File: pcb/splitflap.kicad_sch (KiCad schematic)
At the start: 84 parts, among them J1 Motor D, J10 Hall C, J11 Hall B, J12 I2C, J2 Motor C, J3 Motor B, J4 Motor A, J5 BarrelJack Vertical, J6 USB_C_Receptacle_USB2.0_16P, J7 BarrelJack Horizontal, J8 Hall A1, J9 Hall D, M1 28BYJ-48, SW1 A, SW2 B, SW3 Mode, SW4 RST, U1 ULN2803A, U12 LM2596S-5, U2 ULN2803A, U3 DS18B20, U4 ESP32-S3-WROOM-1, U5 Hall A1, U6 UART, U7 LD1117S33CTR, U8 DCF-77, U9 Hall A2

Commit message: Use 0603 for resistors and capacitors
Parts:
- added R7: 220, Resistor_SMD:R_0603_1608Metric, symbol Device:R
- C1, C10, C11, C12, C13, C14, C15, C17, C7: footprint Capacitor_SMD:C_0805_2012Metric_Pad1.18x1.45mm_HandSolder -> Capacitor_SMD:C_0603_1608Metric
- R1, R5: footprint Resistor_SMD:R_0805_2012Metric_Pad1.20x1.40mm_HandSolder -> Resistor_SMD:R_0603_1608Metric
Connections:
- net +3V3: now also C1.2, C17.2, R1.1, R5.1; no longer C1.1, C17.1, R1.2, R5.2
- net GND: now also C1.1, C17.1; no longer C1.2, C17.2
- net HALL_A1: now also R7.2; no longer R1.1, U5.2 (OUTPUT)
- net HALL_A2: now also R5.2; no longer R5.1
- new net: R1.2, R7.1, U5.2 (OUTPUT)

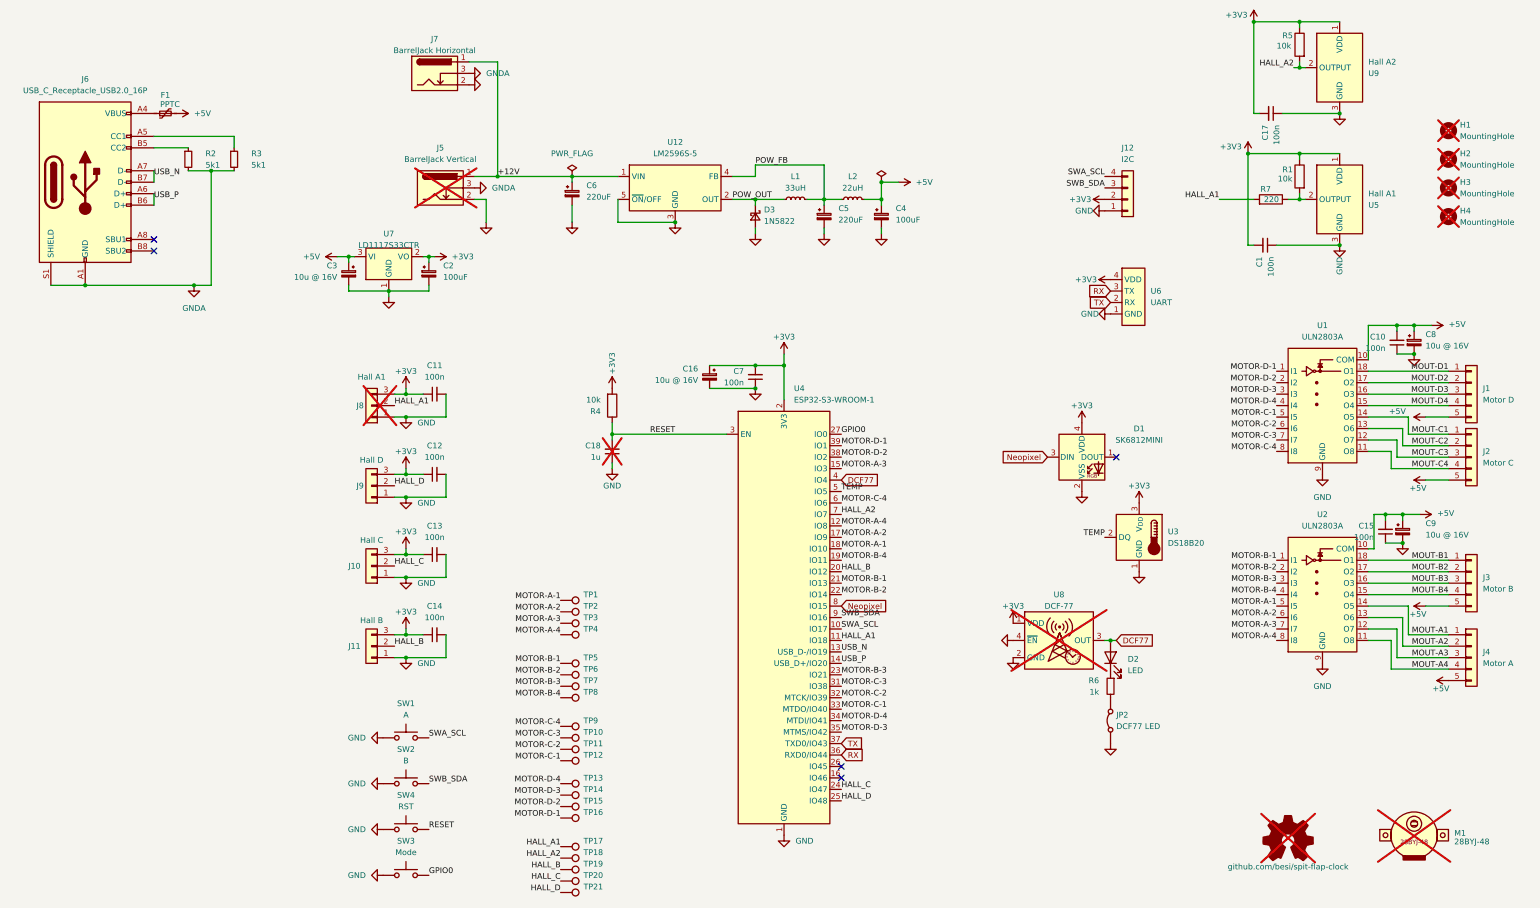
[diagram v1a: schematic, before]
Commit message: Update DNP field
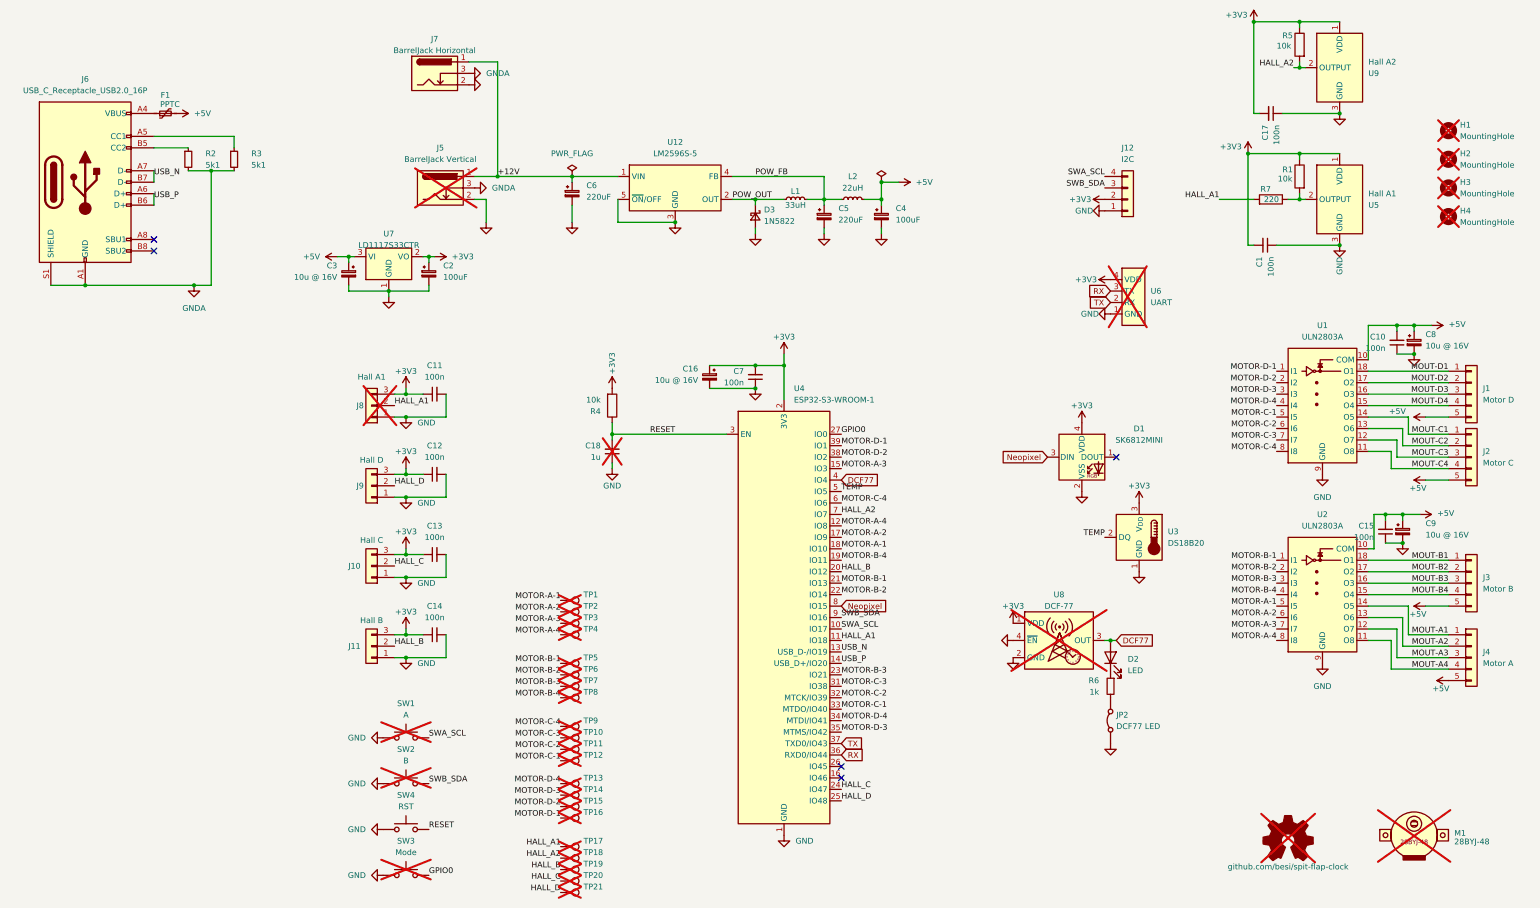
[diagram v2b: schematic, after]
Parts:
- D2, F1, J12, J6, J8, M1, R2, R3, R6, U3, U8: MPN (none) -> (none)
- SW1, SW2, SW3, U6: now not fitted
- TP1, TP10, TP11, TP12, TP13, TP14, TP15, TP16, TP17, TP18, TP19, TP2, TP20, TP21, TP3, TP4, TP5, TP6, TP7, TP8, TP9: MPN (none) -> (none); now not fitted

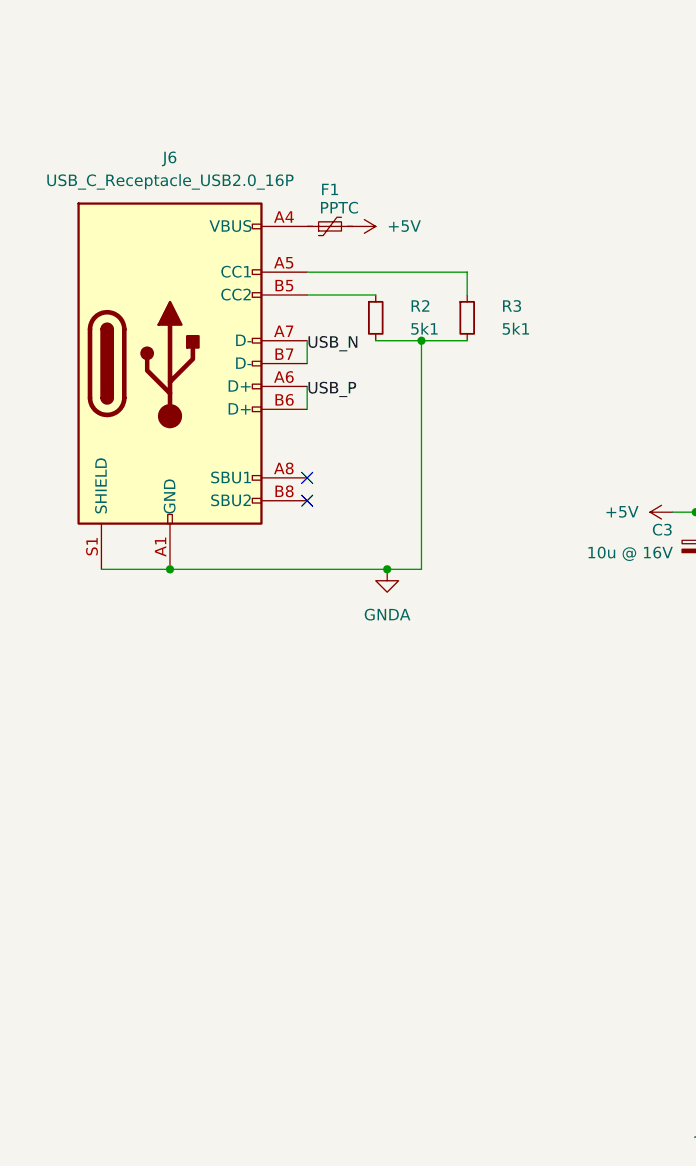
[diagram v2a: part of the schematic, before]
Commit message: Add ESD protection for the USB-C socket
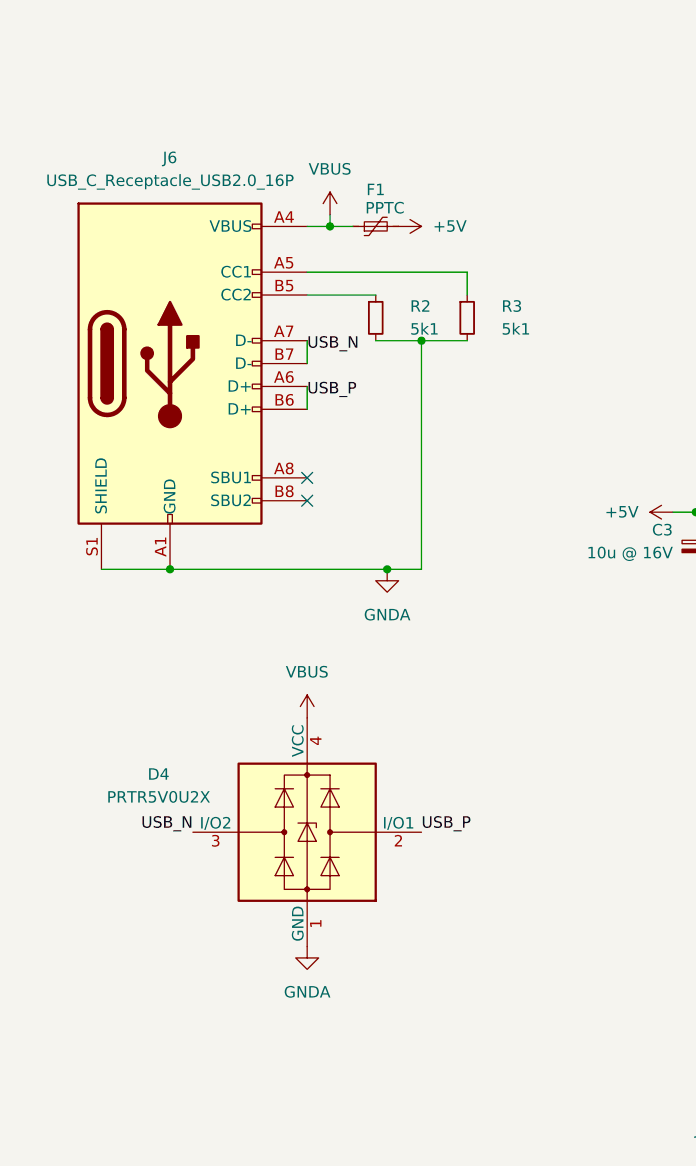
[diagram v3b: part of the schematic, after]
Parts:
- added D4: PRTR5V0U2X, Package_TO_SOT_SMD:SOT-143, symbol Power_Protection:PRTR5V0U2X
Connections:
- net GNDA: now also D4.1 (GND)
- net USB_N: now also D4.3 (I/O2)
- net USB_P: now also D4.2 (I/O1)
- net VBUS: now reaches F1.1, J6.A4 (VBUS), J6.A9 (VBUS), J6.B4 (VBUS), J6.B9 (VBUS)
- net VBUS: now also D4.4 (VCC)
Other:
- moved on the sheet: F1

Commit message: Change package of the temperature sensor
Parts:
- D4: MPN (none) -> PRTR5V0U2X
- J10, J11, J8, J9: MPN (none) -> B3B-PH-K-S
- J12: MPN (none) -> BM04B-SRSS-TB
- M1: MPN (none) -> 28BYJ-48
- SW1, SW2, SW3, SW4: MPN 434133025816 -> PTS815SJM250SMTRLFS
- U1, U2: MPN (none) -> ULN2803A
- U3: footprint Package_TO_SOT_THT:TO-92_Inline_Wide -> Package_TO_SOT_THT:TO-92S; MPN (none) -> 4518-DS18B20-ND
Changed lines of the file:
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@@
 			)
 		)
-		(property "MPN" " "
+		(property "MPN" "28BYJ-48"
 			(at 260.35 172.72 0)
 			(effects
@@
 			)
 		)
-		(property "MPN" "434133025816"
-			(at 36.83 161.29 0)
-			(effects
-				(font
-					(size 1.27 1.27)
-				)
-				(hide yes)
-			)
-		)
-		(property "Label1" ""
-			(at 36.83 161.29 0)
-			(effects
-				(font
-					(size 1.27 1.27)
-				)
-				(hide yes)
-			)
-		)
-		(property "Label2" ""
+		(property "MPN" "PTS815SJM250SMTRLFS"
 			(at 36.83 161.29 0)
 			(effects
@@
 			)
 		)
-		(property "MPN" " "
+		(property "MPN" "ULN2803A"
 			(at 240.03 116.84 0)
 			(effects
@@
 			)
 		)
-		(property "MPN" " "
+		(property "MPN" "B3B-PH-K-S "
 			(at 29.21 113.03 0)
 			(effects
@@
 			)
 		)
-		(property "MPN" "434133025816"
-			(at 36.83 151.13 0)
-			(effects
-				(font
-					(size 1.27 1.27)
-				)
-				(hide yes)
-			)
-		)
-		(property "Label1" ""
-			(at 36.83 151.13 0)
-			(effects
-				(font
-					(size 1.27 1.27)
-				)
-				(hide yes)
-			)
-		)
-		(property "Label2" ""
+		(property "MPN" "PTS815SJM250SMTRLFS"
 			(at 36.83 151.13 0)
 			(effects
@@
 			)
 		)
-		(property "MPN" " "
+		(property "MPN" "B3B-PH-K-S "
 			(at 29.21 130.81 0)
 			(effects
@@
 			)
 		)
-		(property "MPN" " "
+		(property "MPN" "ULN2803A"
 			(at 240.03 74.93 0)
 			(effects
@@
 			)
 		)
-		(property "MPN" " "
+		(property "MPN" "B3B-PH-K-S "
 			(at 29.21 77.47 0)
 			(effects
@@
 			)
 		)
-		(property "Footprint" "Package_TO_SOT_THT:TO-92_Inline_Wide"
+		(property "Footprint" "Package_TO_SOT_THT:TO-92S"
 			(at 224.79 113.03 0)
 			(effects
@@
 			)
 		)
-		(property "MPN" " "
+		(property "MPN" "4518-DS18B20-ND"
 			(at 199.39 106.68 0)
 			(effects
@@
 			)
 		)
+		(property "MPN" "PRTR5V0U2X"
+			(at -19.05 80.01 0)
+			(effects
+				(font
+					(size 1.27 1.27)
+				)
+				(hide yes)
+			)
+		)
 		(pin "4"
 		)
@@
 			)
 		)
-		(property "MPN" "434133025816"
-			(at 36.83 171.45 0)
-			(effects
-				(font
-					(size 1.27 1.27)
-				)
-				(hide yes)
-			)
-		)
-		(property "Label1" ""
-			(at 36.83 171.45 0)
-			(effects
-				(font
-					(size 1.27 1.27)
-				)
-				(hide yes)
-			)
-		)
-		(property "Label2" ""
+		(property "MPN" "PTS815SJM250SMTRLFS"
 			(at 36.83 171.45 0)
 			(effects
@@
 			)
 		)
-		(property "MPN" " "
+		(property "MPN" "B3B-PH-K-S "
 			(at 29.21 95.25 0)
 			(effects
@@
 			)
 		)
-		(property "MPN" " "
+		(property "MPN" "BM04B-SRSS-TB"
 			(at 196.85 31.75 0)
 			(effects
@@
 			)
 		)
-		(property "MPN" "434133025816"
-			(at 36.83 181.61 0)
-			(effects
-				(font
-					(size 1.27 1.27)
-				)
-				(hide yes)
-			)
-		)
-		(property "Label1" ""
-			(at 36.83 181.61 0)
-			(effects
-				(font
-					(size 1.27 1.27)
-				)
-				(hide yes)
-			)
-		)
-		(property "Label2" ""
+		(property "MPN" "PTS815SJM250SMTRLFS"
 			(at 36.83 181.61 0)
 			(effects

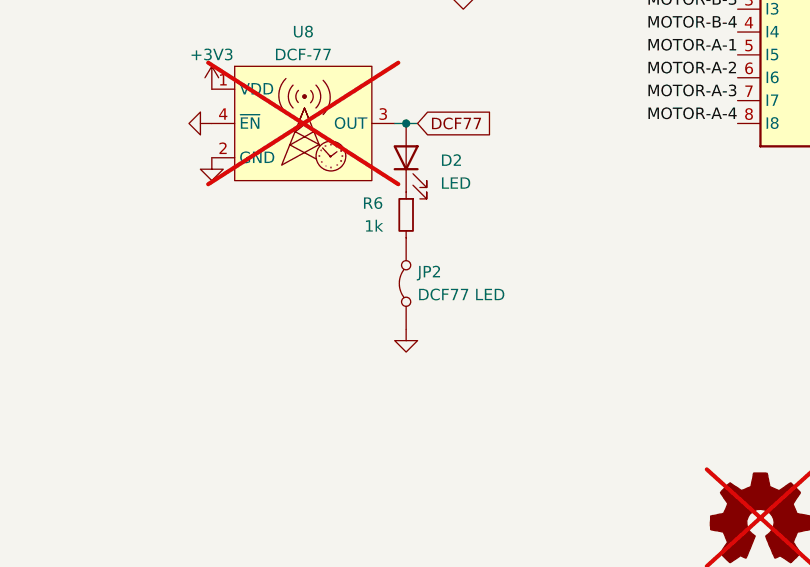
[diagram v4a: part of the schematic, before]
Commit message: Cleanup MPNs
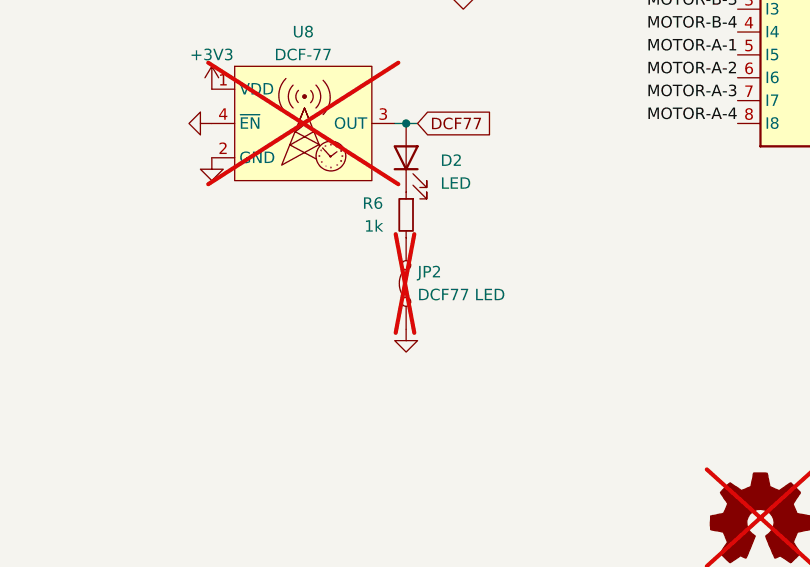
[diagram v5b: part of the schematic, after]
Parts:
- F1: MPN (none) -> MF-NSMF110/16X-2
- J1, J2, J3, J4: MPN (none) -> B5B-XH-A
- J5: MPN (none) -> CP-060A-ND
- J6: MPN (none) -> USB4105-GF-A
- JP2: now not fitted

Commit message: Finalise MPNs
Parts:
- C1, C10, C11, C12, C13, C14, C15, C17, C7: MPN (none) -> CL10E104KC8VPNC
- C18: MPN (none) -> CL21B105KOFNNNG
- D2: MPN (none) -> 150060RS75000
- H1, H2, H3, H4, JP2, OSHW1, TP1, TP10, TP11, TP12, TP13, TP14, TP15, TP16, TP17, TP18, TP19, TP2, TP20, TP21, TP3, TP4, TP5, TP6, TP7, TP8, TP9, U6, U8: MPN (none) -> X
- J7: MPN (none) -> 2073-DCJ200-10-A-K1-K-ND
- R1, R4, R5: MPN (none) -> CR0603-FX-1002ELF
- R2, R3: MPN (none) -> CR0603-FX-5101ELF
- R6: MPN (none) -> CR0603-JW-102ELF
- R7: MPN (none) -> CR0603-JW-221ELF

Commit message: Finalise the part’s MPN
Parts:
- D3: MPN 1N5822 -> 497-11370-1-ND
- U1, U2: MPN ULN2803A -> 4518-ULN2803ATR-ND
- U12: MPN LM2596S-5.0 -> 5399-LM2596S-5.0CT-ND

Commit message: Unambiguous MPN for the TVS diode array
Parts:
- D4: MPN PRTR5V0U2X -> PRTR5V0U2X,215
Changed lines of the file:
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@@
 			)
 		)
-		(property "MPN" "PRTR5V0U2X"
+		(property "MPN" "PRTR5V0U2X,215"
 			(at -19.05 80.01 0)
 			(effects
